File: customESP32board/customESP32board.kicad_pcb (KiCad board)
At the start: 2 copper layers, 60 x 65 mm, 49 parts, among them J1 USB_B, J2 Conn_01x16_Pin, J3 Conn_01x16_Pin, Q1 S8050, Q2 S8050, Q3 BSS138, Q4 BSS138, Q5 BSS138, SW1 SW_Push, SW2 SW_Push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

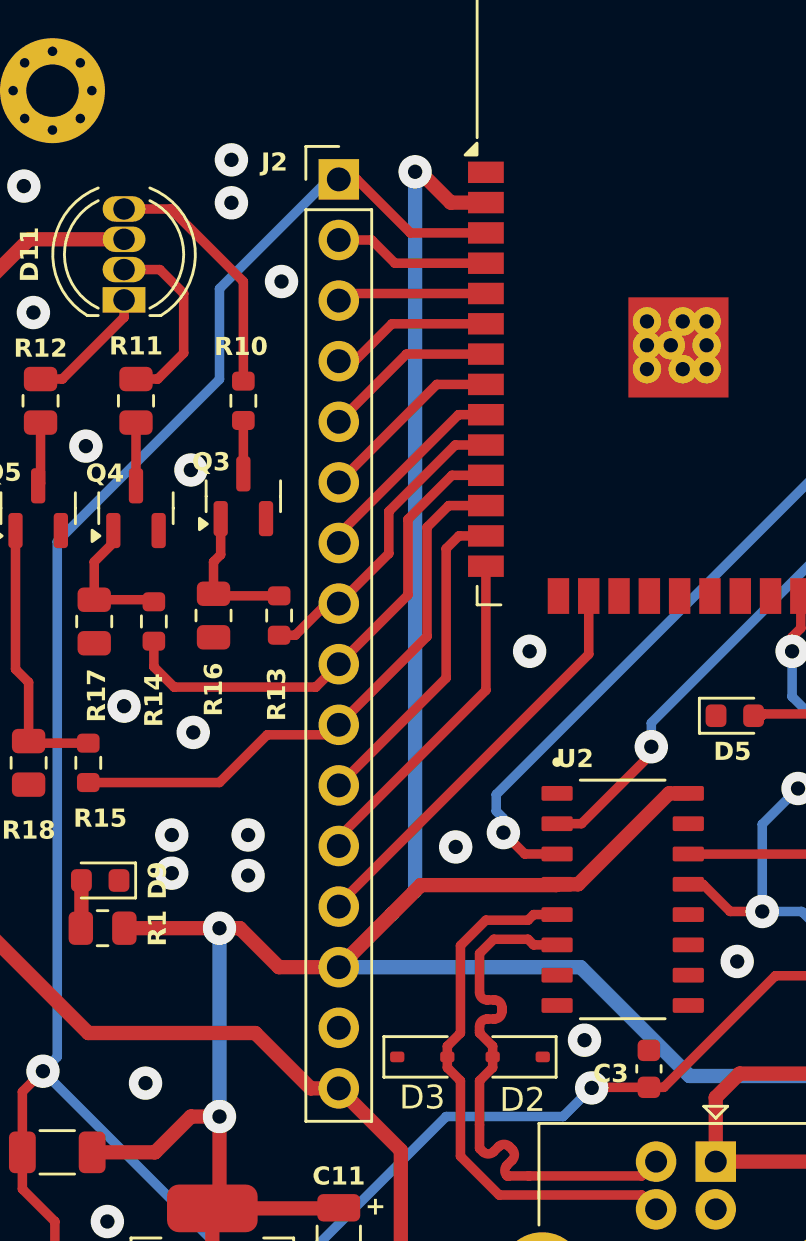
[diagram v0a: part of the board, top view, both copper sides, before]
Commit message: updated PCB layout placement
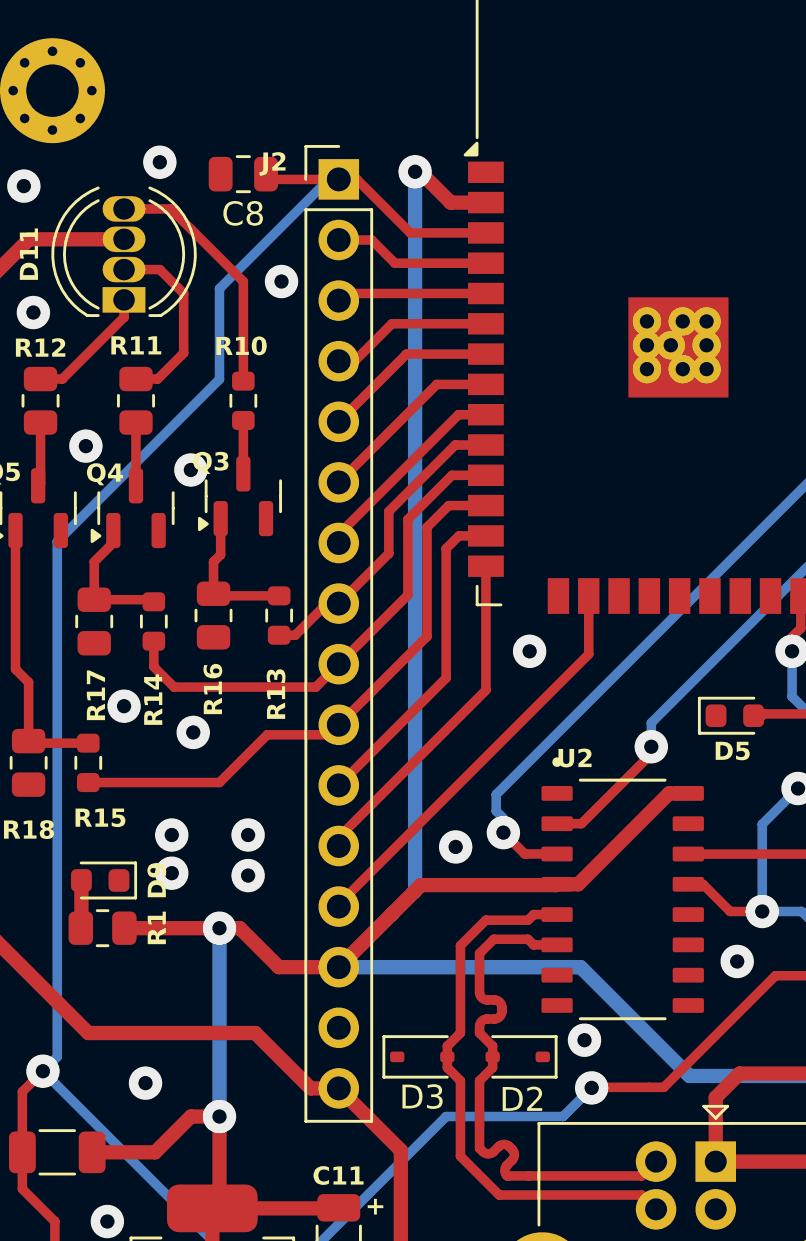
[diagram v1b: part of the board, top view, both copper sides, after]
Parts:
- removed C3: 0.1uF, 10V, Capacitor_SMD:C_0603_1608Metric
- added C8: 10uF, 25V, Capacitor_SMD:C_0805_2012Metric, F.Cu at (117.5, 82.0)
- R5, R6: value 10 Ohm -> 10K Ohm
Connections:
- Q1 pad 1: ESP_EN -> RTS
- Q1 pad 3: RTS -> ESP_EN
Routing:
- net ESP_EN: track 99.9 -> 103.0 mm
- net GND: vias 50 -> 49

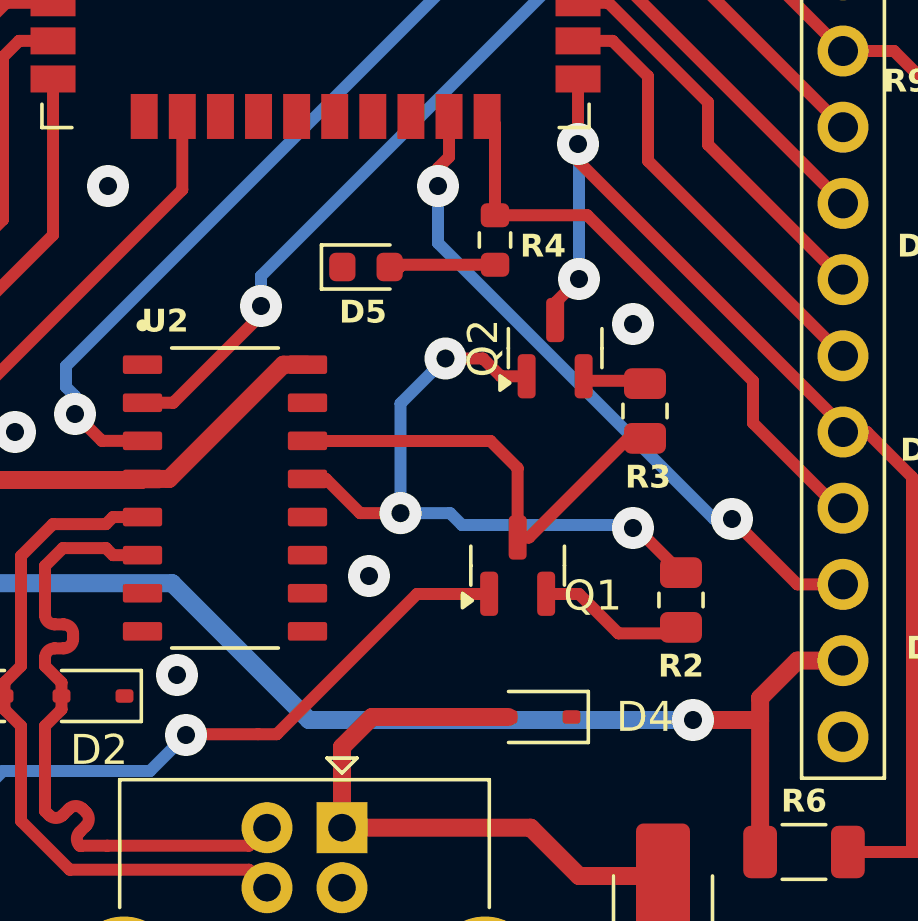
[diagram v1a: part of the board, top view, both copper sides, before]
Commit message: updated PCB layout
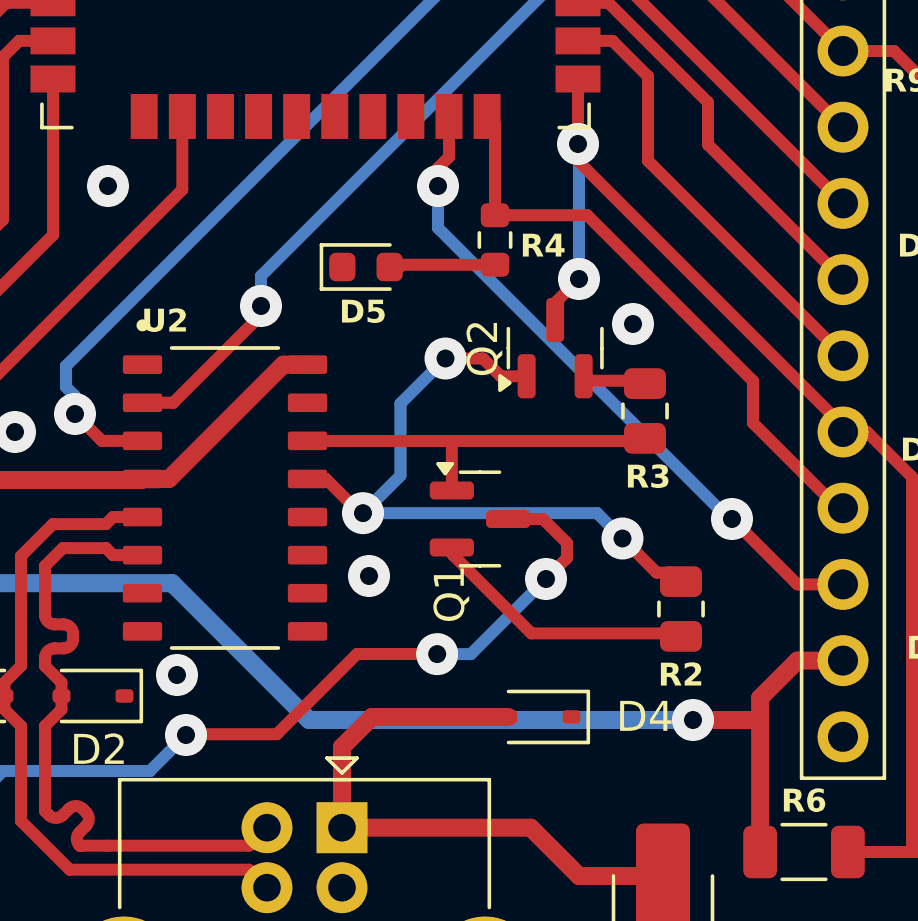
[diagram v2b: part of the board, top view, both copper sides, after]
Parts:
- moved Q1 2.00 mm to (141.9, 113.1), turned to 0 degrees
- moved R2 0.30 mm to (148.6, 116.1)
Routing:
- net ESP_EN: track 103.0 -> 109.2 mm, vias 2 -> 4
- net Net-(Q1-B): track 5.12 -> 8.99 mm
- net RTS: track 15.4 -> 14.5 mm
- net DTR: track 22.6 -> 23.1 mm

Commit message: updated routing
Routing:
- net Net-(Q1-B): track 8.99 -> 9.65 mm
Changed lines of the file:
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@@
 		(capping no)
 		(filling no)
-		(zone_defaults)
 		(aux_axis_origin 104.5 73.5)
 		(grid_origin 104.5 73.5)
@@
 	)
 	(segment
-		(start 148.6 117.0125)
-		(end 148.5 117.0125)
+		(start 140.8 114.2125)
+		(end 140.9625 114.05)
 		(width 0.4)
 		(layer "F.Cu")
@@
 	)
 	(segment
-		(start 141 114.3)
-		(end 141 114.0875)
+		(start 148.5 117.0125)
+		(end 148.4 116.9125)
 		(width 0.4)
 		(layer "F.Cu")
@@
 	)
 	(segment
-		(start 148.4 116.9125)
-		(end 143.6125 116.9125)
+		(start 142.7125 116.9125)
+		(end 140.8 115)
 		(width 0.4)
 		(layer "F.Cu")
@@
 	)
 	(segment
-		(start 148.5 117.0125)
-		(end 148.4 116.9125)
+		(start 148.4 116.9125)
+		(end 142.7125 116.9125)
 		(width 0.4)
 		(layer "F.Cu")
@@
 	)
 	(segment
-		(start 143.6125 116.9125)
-		(end 141 114.3)
+		(start 148.6 117.0125)
+		(end 148.5 117.0125)
 		(width 0.4)
 		(layer "F.Cu")
@@
 	)
 	(segment
-		(start 141 114.0875)
-		(end 140.9625 114.05)
+		(start 140.8 115)
+		(end 140.8 114.2125)
 		(width 0.4)
 		(layer "F.Cu")
@@
 	)
 	(segment
+		(start 143.5 113.1)
+		(end 142.8375 113.1)
+		(width 0.4)
+		(layer "F.Cu")
+		(net "ESP_EN")
+	)
+	(segment
 		(start 109.1 119.6)
 		(end 108.2375 120.4625)
@@
 	)
 	(segment
+		(start 144 114.8)
+		(end 144 114.5)
+		(width 0.4)
+		(layer "F.Cu")
+		(net "ESP_EN")
+	)
+	(segment
 		(start 108.2375 124.5375)
 		(end 109.6 125.9)
@@
 	)
 	(segment
-		(start 144 113.1)
-		(end 142.8375 113.1)
+		(start 144 114.5)
+		(end 144.1 114.4)
 		(width 0.4)
 		(layer "F.Cu")
@@
 	)
 	(segment
-		(start 144.8 113.9)
-		(end 144 113.1)
+		(start 121.5 82.22)
+		(end 122.2575 82.22)
 		(width 0.4)
 		(layer "F.Cu")
@@
 	)
 	(segment
-		(start 121.5 82.22)
-		(end 122.2575 82.22)
+		(start 144.1 114.4)
+		(end 144.1 113.7)
 		(width 0.4)
 		(layer "F.Cu")
@@
 	)
 	(segment
+		(start 144.1 113.7)
+		(end 143.5 113.1)
+		(width 0.4)
+		(layer "F.Cu")
+		(net "ESP_EN")
+	)
+	(segment
 		(start 108.2375 123)
 		(end 108.2375 124.5375)
@@
 	)
 	(segment
-		(start 144.8 114.4)
-		(end 144.8 113.9)
-		(width 0.4)
-		(layer "F.Cu")
-		(net "ESP_EN")
-	)
-	(segment
 		(start 132.625 120.275)
 		(end 132.6 120.3)
@@
 		(net "ESP_EN")
 	)
-	(segment
-		(start 144.1 115.1)
-		(end 144.8 114.4)
-		(width 0.4)
-		(layer "F.Cu")
-		(net "ESP_EN")
-	)
 	(via
 		(at 132.1 120.3)
@@
 	)
 	(via
-		(at 140.472896 117.60386)
+		(at 139.7 117.6)
 		(size 1.4)
 		(drill 0.6)
@@
 	)
 	(via
-		(at 144.1 115.1)
+		(at 144 114.8)
 		(size 1.4)
 		(drill 0.6)
@@
 	)
 	(segment
+		(start 139.70386 117.60386)
+		(end 139.7 117.6)
+		(width 0.4)
+		(layer "B.Cu")
+		(net "ESP_EN")
+	)
+	(segment
 		(start 109.7 97.4)
 		(end 116.5 90.6)
@@
 	)
 	(segment
+		(start 144 114.8)
+		(end 144 115.3)
+		(width 0.4)
+		(layer "B.Cu")
+		(net "ESP_EN")
+	)
+	(segment
 		(start 121.08 82.22)
 		(end 121.5 82.22)
@@
 	)
 	(segment
-		(start 144.1 115.1)
-		(end 141.59614 117.60386)
+		(start 116.5 90.6)
+		(end 116.5 86.8)
 		(width 0.4)
 		(layer "B.Cu")
@@
 	)
 	(segment
-		(start 116.5 90.6)
-		(end 116.5 86.8)
+		(start 143.8 115.4)
+		(end 141.59614 117.60386)
 		(width 0.4)
 		(layer "B.Cu")
@@
 	)
 	(segment
-		(start 141.59614 117.60386)
-		(end 140.472896 117.60386)
+		(start 109.7 119)
+		(end 109.7 97.4)
 		(width 0.4)
 		(layer "B.Cu")
@@
 	)
 	(segment
-		(start 109.7 119)
-		(end 109.7 97.4)
+		(start 144 115.3)
+		(end 143.9 115.4)
+		(width 0.4)
+		(layer "B.Cu")
+		(net "ESP_EN")
+	)
+	(segment
+		(start 143.9 115.4)
+		(end 143.8 115.4)
 		(width 0.4)
 		(layer "B.Cu")
@@
 		(width 0.4)
 		(layer "B.Cu")
+		(net "ESP_EN")
+	)
+	(segment
+		(start 141.59614 117.60386)
+		(end 139.70386 117.60386)
+		(width 0.4)
+		(layer "B.Cu")
